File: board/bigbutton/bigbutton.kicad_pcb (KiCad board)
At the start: 2 copper layers, 58 x 64 mm, 57 parts, among them J1 SWD, J2 USB_C_Receptacle_USB2.0, SW1 RESET, SW2 SMOL, SW3 LORGE, SW4 BOOT0, U1 STM32F302CBTx, U2 ATECC608A-SSHDA, U3 USBLC6-2, U4 SN74LV1T34DBV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

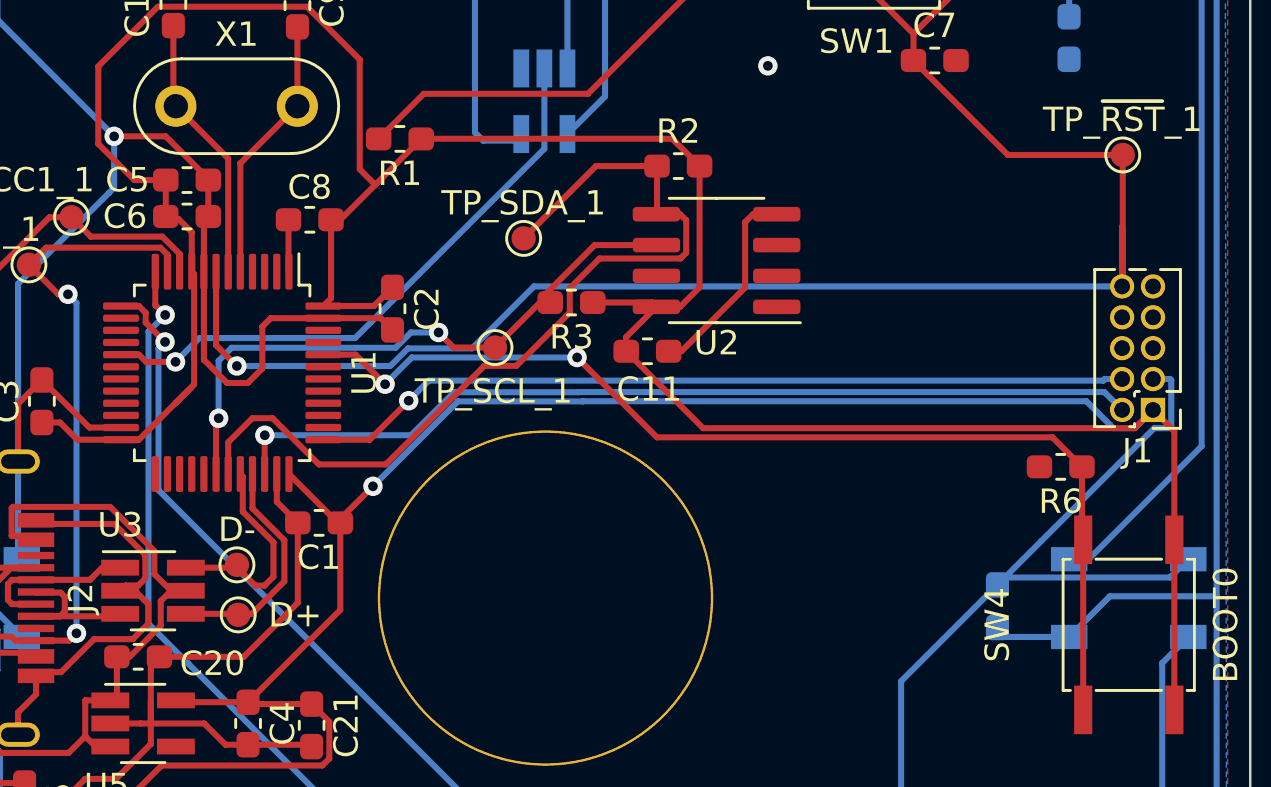
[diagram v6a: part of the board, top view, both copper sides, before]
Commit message: Switch to pin-compatible STM32F303CBT6, as reflected in order
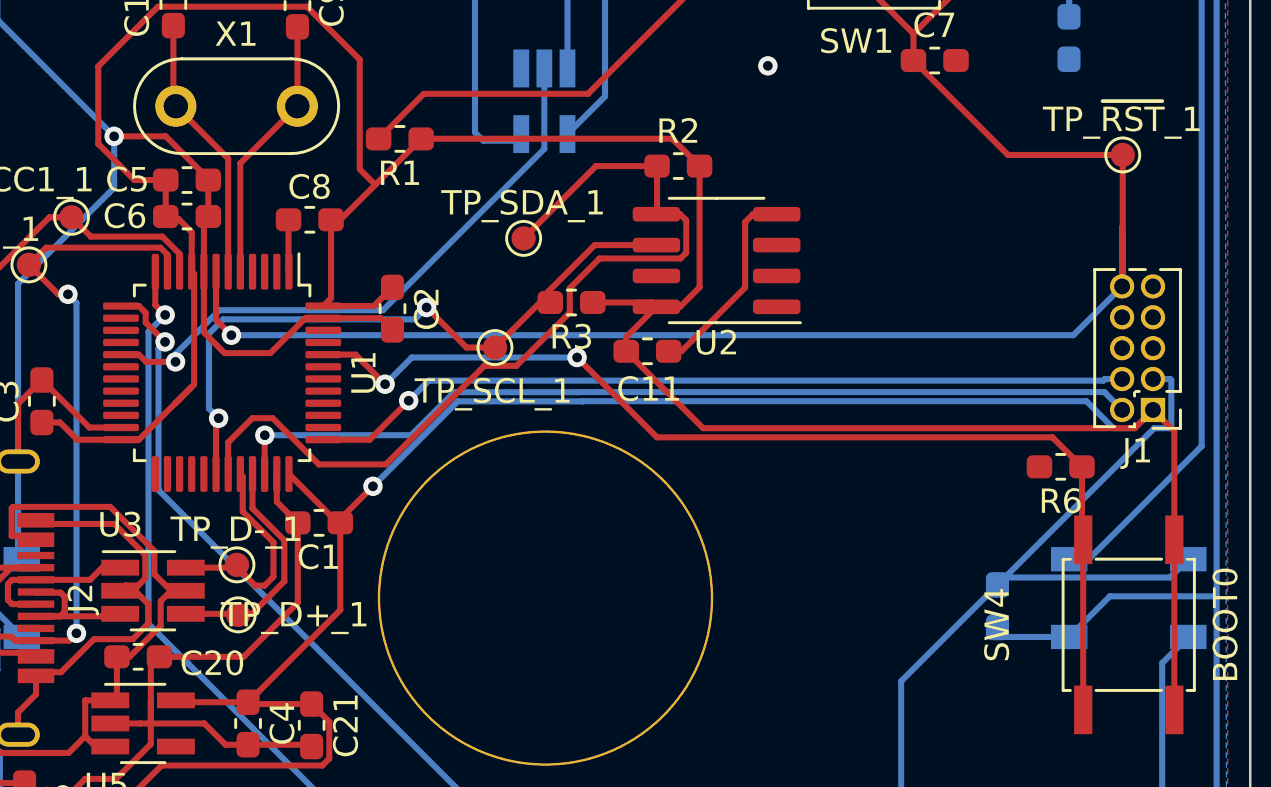
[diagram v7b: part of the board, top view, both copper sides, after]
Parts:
- U1: value STM32F302CBTx -> STM32F303CBTx
- renumbered D+ to TP_D+_1, D- to TP_D-_1
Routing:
- net GND: track 251.9 -> 249.2 mm
- net /I2C_SCL: track 25.6 -> 27.7 mm
- net /~RST: track 89.2 -> 87.6 mm

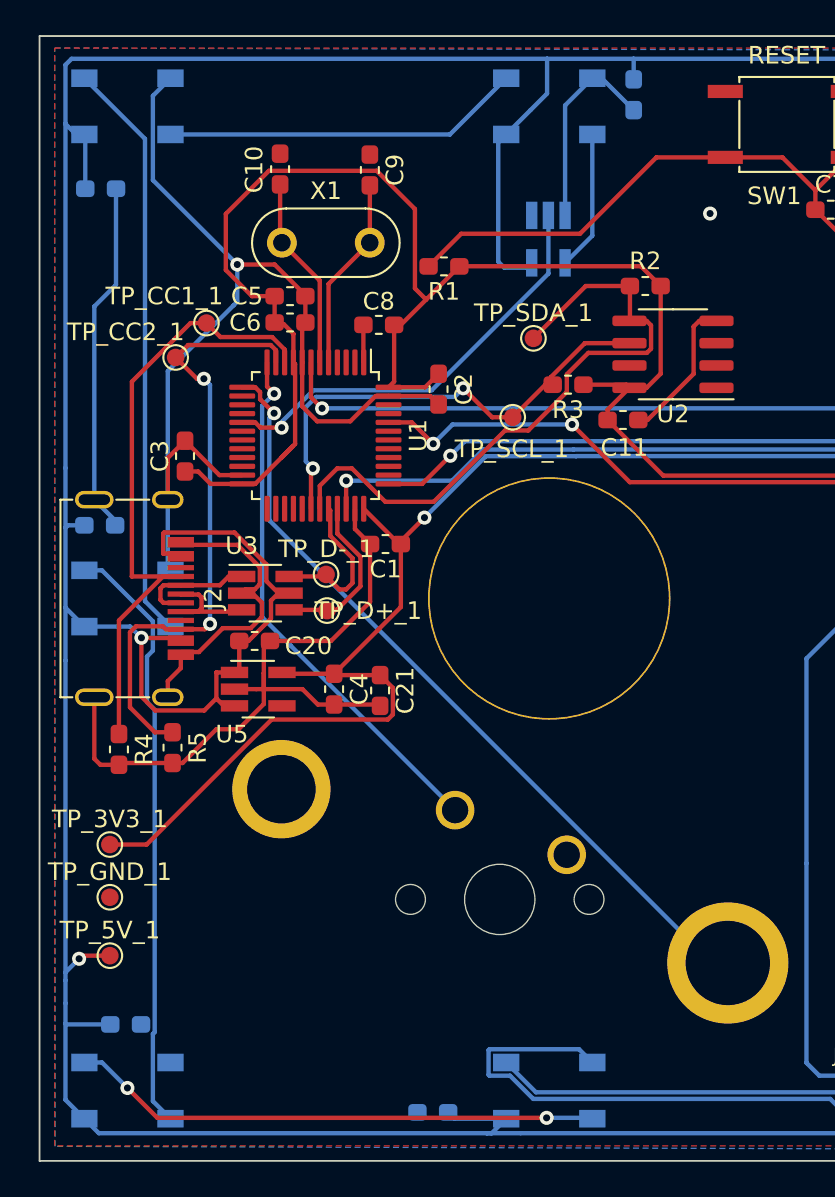
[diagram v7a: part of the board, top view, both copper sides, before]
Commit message: Switch to a top-mount USB connector from an incorrect mid-mount
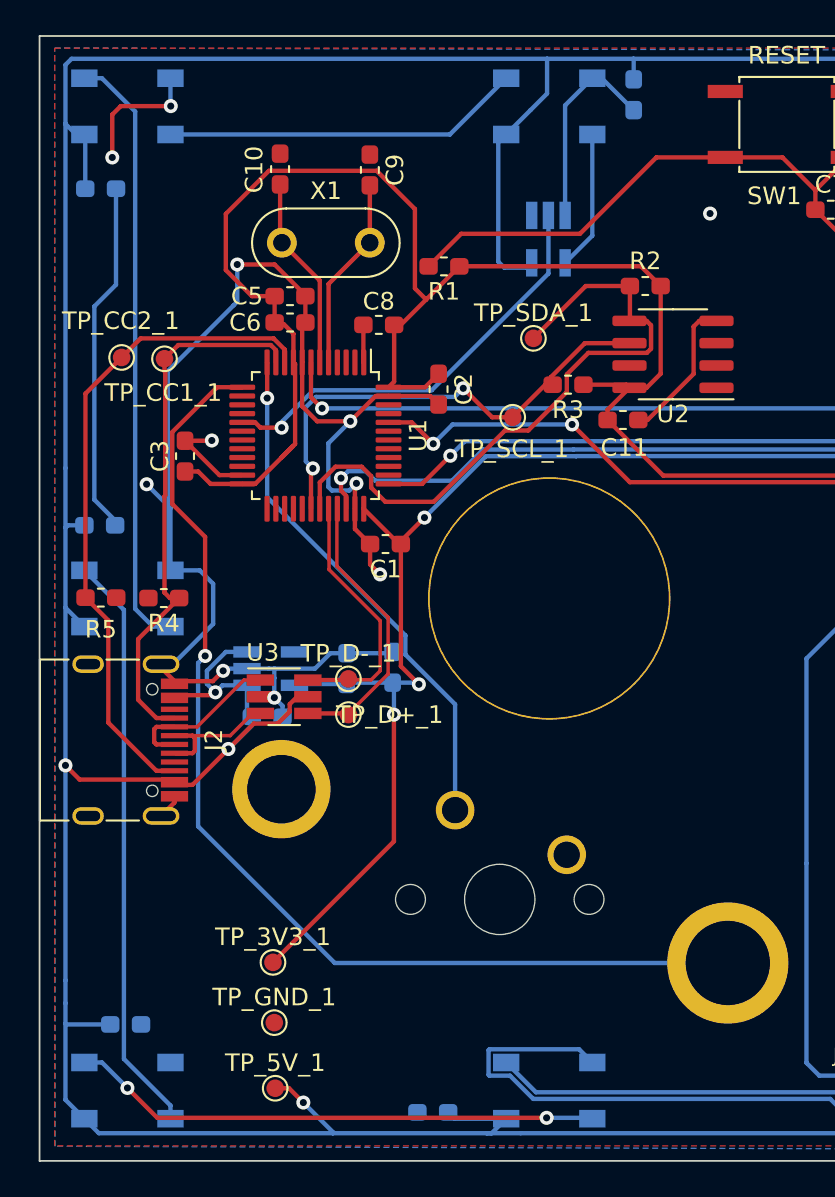
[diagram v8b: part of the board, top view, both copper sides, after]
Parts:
- C20, C21, C4, U5: moved to B.Cu
- J2: footprint bigbutton:USB_C_Receptacle_HRO_TYPE-C-31-M-13_handsolder -> bigbutton:USB_C_Receptacle_JING_C167321_HandSolder
- moved TP_5V_1 12.1 mm to (89.4, 132.9)
- moved TP_GND_1 11.8 mm to (89.4, 129.1)
- moved TP_3V3_1 11.4 mm to (89.3, 125.7)
- moved R5 9.46 mm to (79.5, 105.0), turned to 0 degrees
- moved R4 8.98 mm to (83.1, 105.0), turned to 180 degrees
- moved J2 8.35 mm to (79.8, 113.1)
- moved TP_D-_1 6.08 mm to (93.6, 109.6)
- moved TP_D+_1 6.04 mm to (93.6, 111.6)
- moved U3 5.99 mm to (89.9, 110.6)
- moved C20 4.38 mm to (89.0, 111.7)
- moved TP_CC1_1 3.14 mm to (83.1, 91.4)
- moved TP_CC2_1 3.07 mm to (80.7, 91.3)
- moved C21 1.50 mm to (96.1, 108.9), turned to 90 degrees
- moved C4 1.37 mm to (93.5, 109.0), turned to 90 degrees
- moved U5 1.37 mm to (89.2, 109.0)
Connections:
- U1 pad 10: /USB_CC1 -> /USB_CC2
- U1 pad 11: /USB_CC2 -> /USB_CC1
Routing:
- net GND: track 249.2 -> 229.5 mm, vias 2 -> 11
- net Net-(SW3-Pad1): track 45.4 -> 61.8 mm
- net /USB_D+: track 9.57 -> 16.1 mm
- net /USB_D-: track 8.87 -> 14.8 mm
- net /USB_CC1: track 36.3 -> 31.0 mm
- net +5V: track 321.7 -> 317.3 mm, vias 2 -> 4
- net /USB_CC2: track 35.2 -> 37.8 mm, vias 2 -> 0
- net /USB_UNFILTERED_D-: track 6.78 -> 9.15 mm
- net /USB_UNFILTERED_D+: track 6.64 -> 8.57 mm
- net +3V3: track 190.2 -> 188.3 mm, vias 1 -> 3
- net Net-(D2-Pad2): track 33.2 -> 34.4 mm
- net /SWDIO: track 37.9 -> 38.9 mm
- net Net-(D3-Pad2): track 34.2 -> 33.2 mm
- net Net-(SW2-Pad1): track 30.6 -> 29.9 mm
- net /I2C_SDA: track 36.9 -> 37.5 mm
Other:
- rule trace_min: 0.25 -> 0.2
